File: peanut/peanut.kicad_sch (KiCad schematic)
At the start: 35 parts, among them J1 USB-C, Q1 NMOS, U2 MS5611-01BA, U3 ESP32-C3FH4, Y2 40MHz

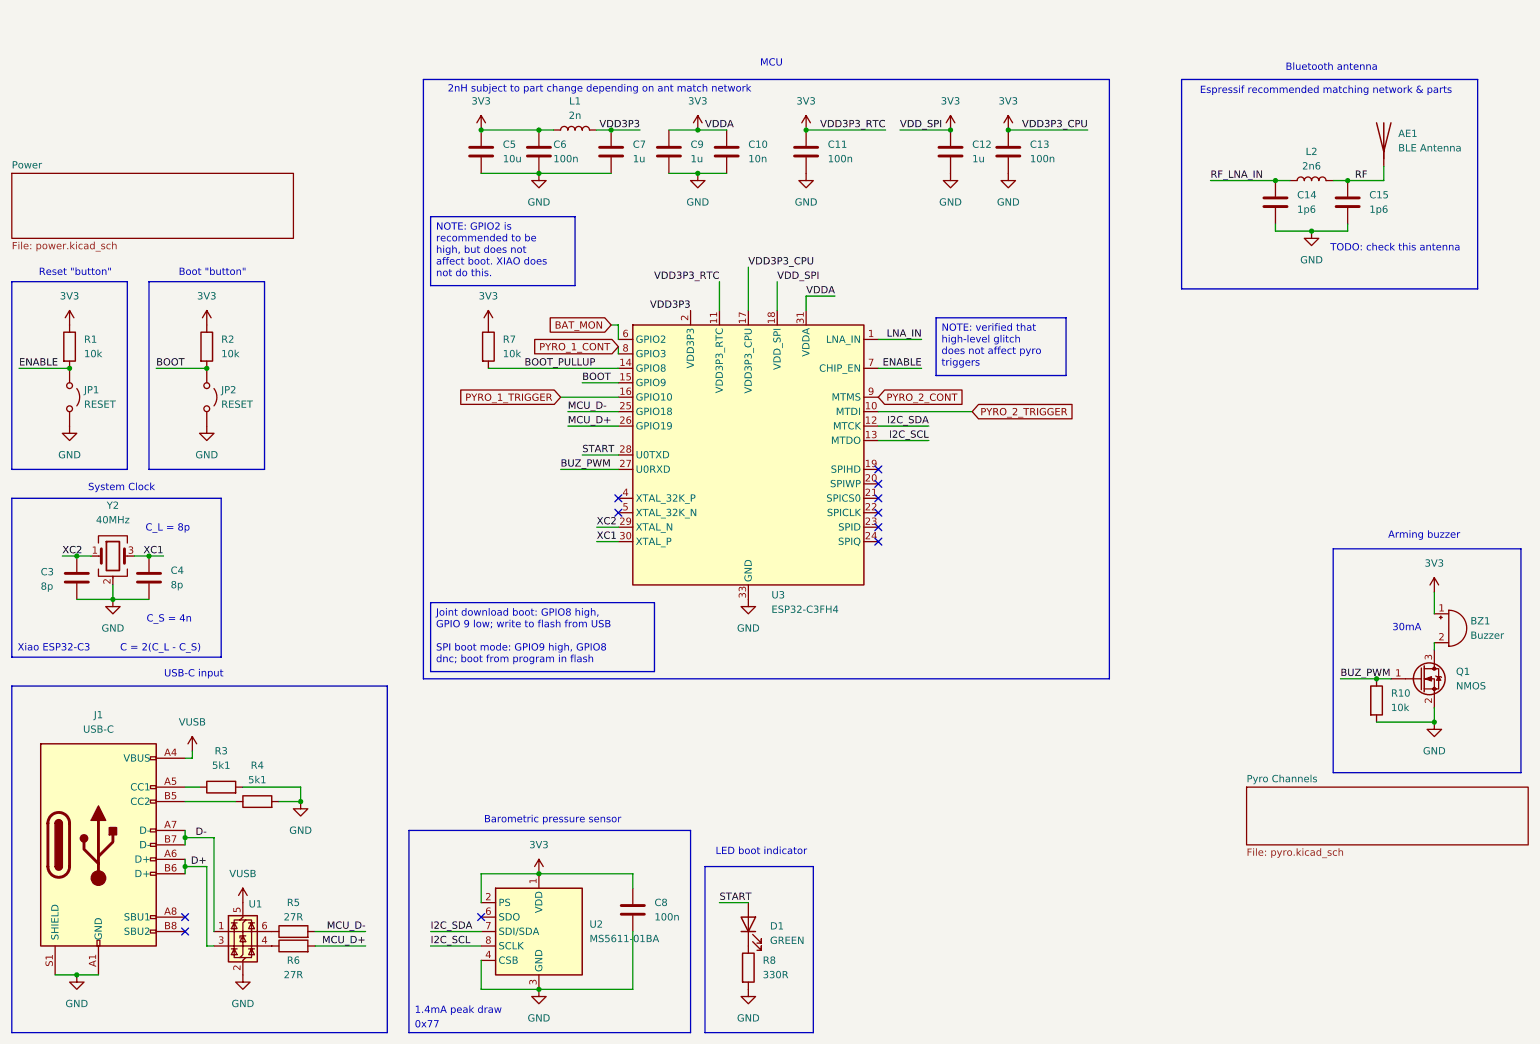
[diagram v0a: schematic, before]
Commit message: feat: Mounting holes
Added M3 mounting holes.
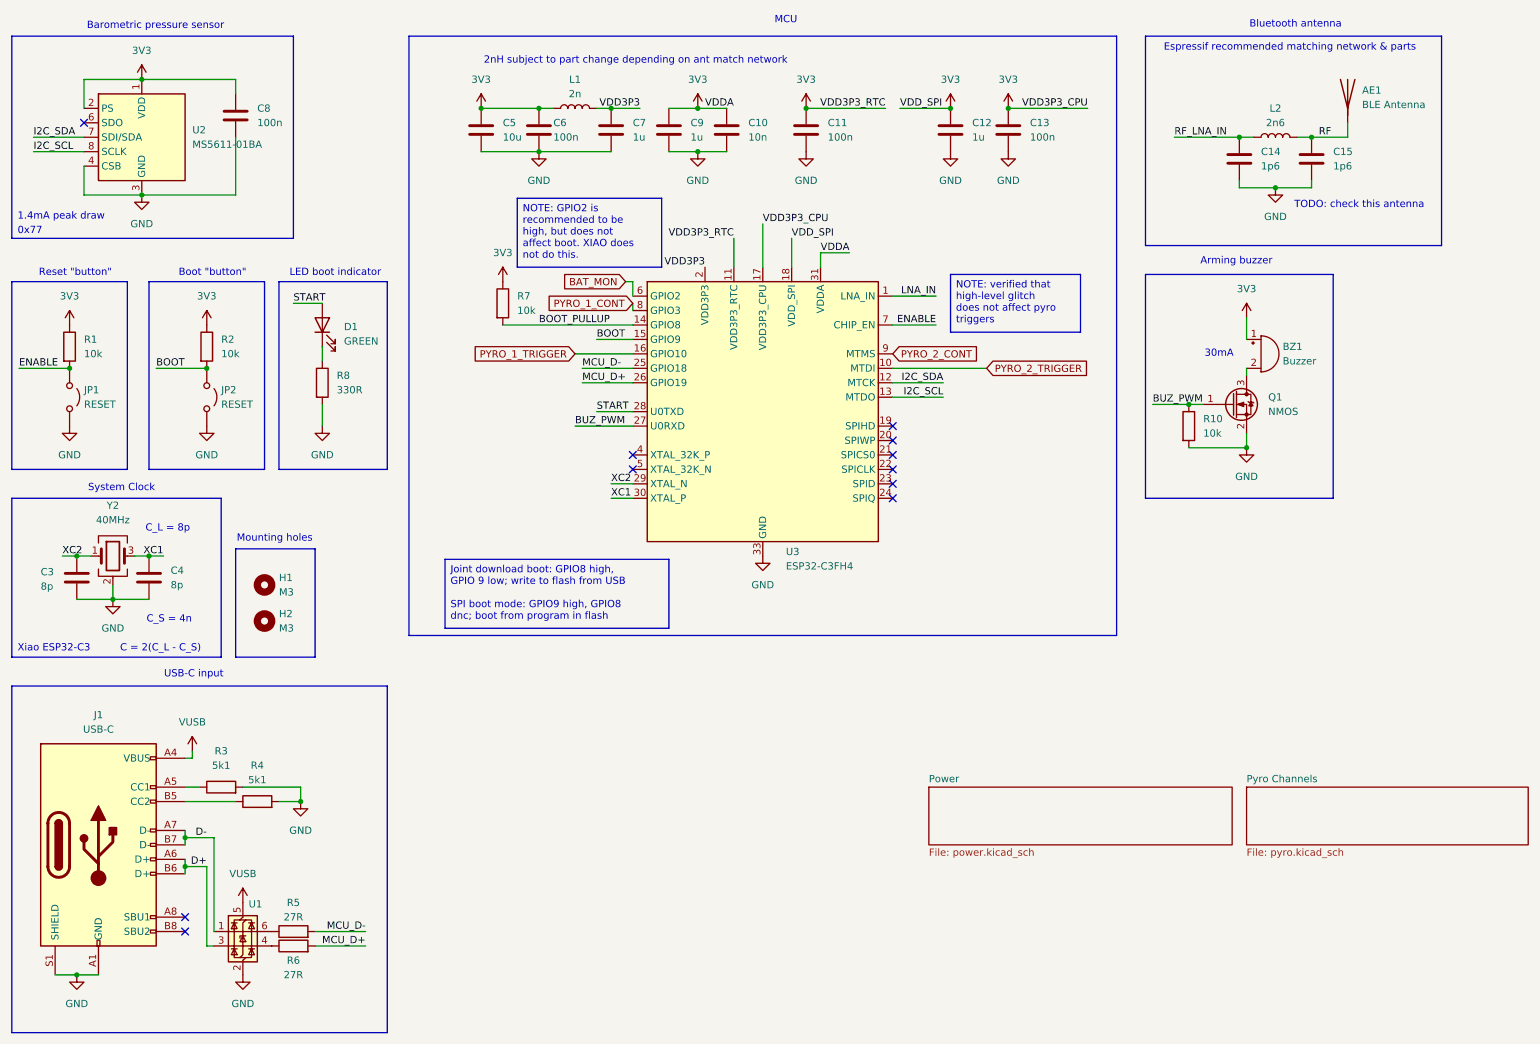
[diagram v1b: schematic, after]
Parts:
- added H1, H2: M3, MountingHole:MountingHole_3.2mm_M3_DIN965_Pad_TopOnly, symbol Mechanical:MountingHole
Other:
- note added: "Mounting holes"
- moved on the sheet: AE1, BZ1, C10, C11, C12, C13, C14, C15, C5, C6, C7, C8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

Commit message: feat: Better layout
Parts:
- renumbered C3 to C1, C12 to C10, C13 to C11, C14 to C12, C15 to C13, C4 to C2, C8 to C3, C5 to C4, C6 to C5, C7 to C6, C9 to C7, C10 to C8, C11 to C9, R8 to R7, R7 to R8, R10 to R9, U2 to U1, U1 to U2, Y2 to Y1
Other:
- note added: "M3 mounting"
- note removed: "Mounting holes"
- moved on the sheet: H1, H2

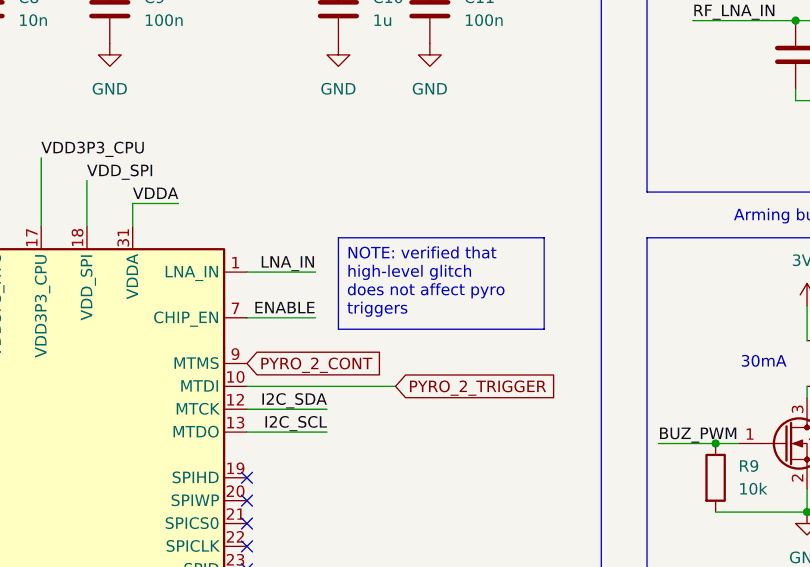
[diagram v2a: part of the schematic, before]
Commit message: feat: Added necessary silkscreen information
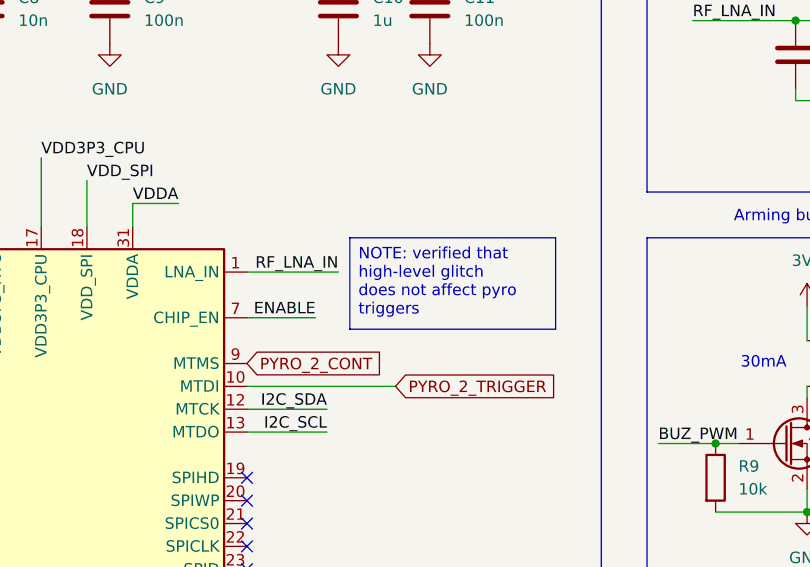
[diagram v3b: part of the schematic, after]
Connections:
- net LNA_IN is gone; now on net RF_LNA_IN: U3.1 (LNA_IN)
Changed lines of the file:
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@@
 	(text_box "NOTE: verified that high-level glitch does not affect pyro triggers"
 		(exclude_from_sim no)
-		(at 180.34 62.23 0)
+		(at 181.61 62.23 0)
 		(size 22.86 10.16)
 		(margins 0.9525 0.9525 0.9525 0.9525)
@@
 	(wire
 		(pts
-			(xy 177.8 66.04) (xy 170.18 66.04)
+			(xy 180.34 66.04) (xy 170.18 66.04)
 		)
 		(stroke
@@
 		)
 	)
-	(label "LNA_IN"
-		(at 177.8 66.04 180)
-		(effects
-			(font
+	(label "RF_LNA_IN"
+		(at 180.34 66.04 180)
+		(effects
+			(font

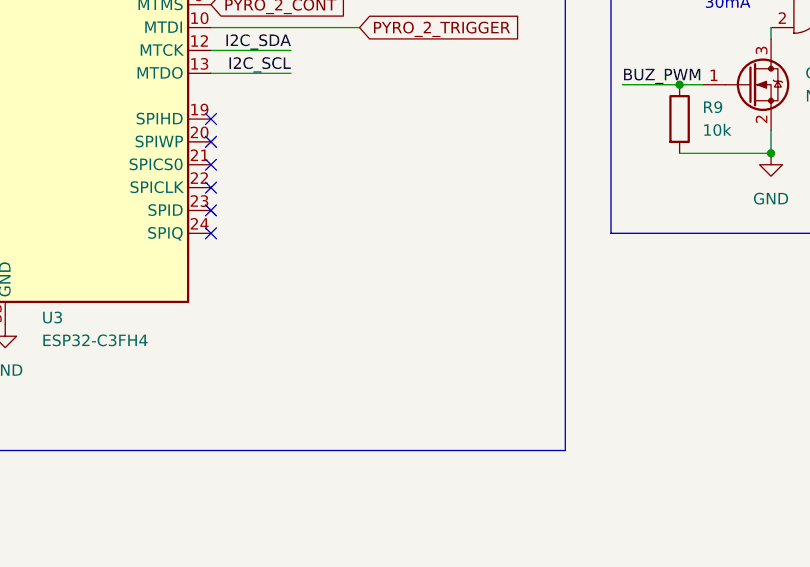
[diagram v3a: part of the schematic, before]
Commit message: feat: Added inner layer pours
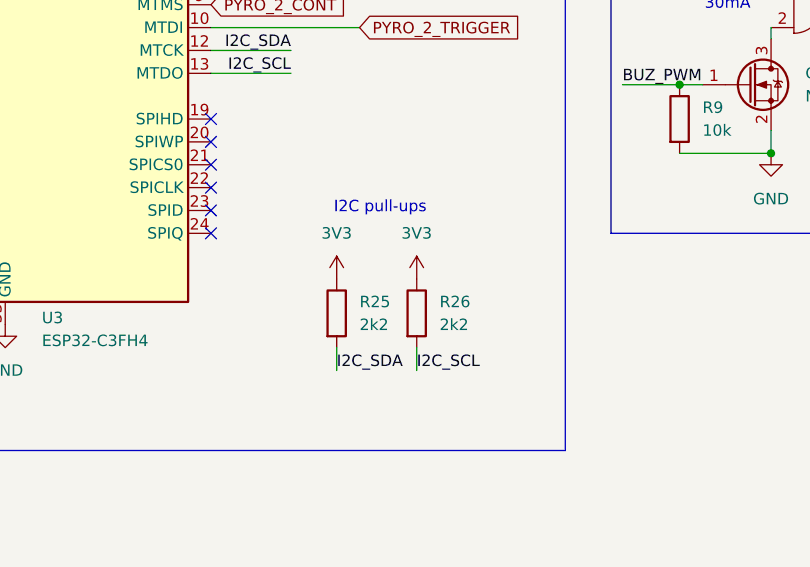
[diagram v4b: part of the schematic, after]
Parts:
- added R25, R26: 2k2, Resistor_SMD:R_0402_1005Metric, symbol Device:R
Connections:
- net 3V3: now also R25.1, R26.1
- net I2C_SCL: now also R26.2
- net I2C_SDA: now also R25.2
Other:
- note added: "I2C pull-ups"

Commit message: feat: 100n capacitors to 0603
Since there is sufficient space, the 100n capacitors have been increased
to 0603 size and all placed on the back of the board. This allows the
board to be squished in further slightly.
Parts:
- C11, C3, C5, C9: footprint Capacitor_SMD:C_0402_1005Metric -> Capacitor_SMD:C_0603_1608Metric; MPN GRM155R61A104KA01J -> KGM15AR70J104KT
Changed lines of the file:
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@@
 			)
 		)
-		(property "Footprint" "Capacitor_SMD:C_0402_1005Metric"
+		(property "Footprint" "Capacitor_SMD:C_0603_1608Metric"
 			(at 191.4652 40.64 0)
 			(hide yes)
@@
 			)
 		)
-		(property "Datasheet" ""
+		(property "Datasheet" "https://ele.kyocera.com/assets/products/capacitor/KGM_Series_e.pdf"
 			(at 190.5 36.83 0)
 			(hide yes)
@@
 			)
 		)
-		(property "MPN" "GRM155R61A104KA01J"
+		(property "MPN" "KGM15AR70J104KT"
 			(at 190.5 36.83 0)
 			(hide yes)
@@
 			)
 		)
-		(property "Footprint" "Capacitor_SMD:C_0402_1005Metric"
+		(property "Footprint" "Capacitor_SMD:C_0603_1608Metric"
 			(at 155.9052 40.64 0)
 			(hide yes)
@@
 			)
 		)
-		(property "Datasheet" ""
+		(property "Datasheet" "https://ele.kyocera.com/assets/products/capacitor/KGM_Series_e.pdf"
 			(at 154.94 36.83 0)
 			(hide yes)
@@
 			)
 		)
-		(property "MPN" "GRM155R61A104KA01J"
+		(property "MPN" "KGM15AR70J104KT"
 			(at 154.94 36.83 0)
 			(hide yes)
@@
 			)
 		)
-		(property "Footprint" "Capacitor_SMD:C_0402_1005Metric"
+		(property "Footprint" "Capacitor_SMD:C_0603_1608Metric"
 			(at 55.5752 38.1 0)
 			(hide yes)
@@
 			)
 		)
-		(property "Datasheet" ""
+		(property "Datasheet" "https://ele.kyocera.com/assets/products/capacitor/KGM_Series_e.pdf"
 			(at 54.61 34.29 0)
 			(hide yes)
@@
 			)
 		)
-		(property "MPN" "GRM155R61A104KA01J"
+		(property "MPN" "KGM15AR70J104KT"
 			(at 54.61 34.29 0)
 			(hide yes)
@@
 			)
 		)
-		(property "Footprint" "Capacitor_SMD:C_0402_1005Metric"
+		(property "Footprint" "Capacitor_SMD:C_0603_1608Metric"
 			(at 108.9152 40.64 0)
 			(hide yes)
@@
 			)
 		)
-		(property "Datasheet" ""
+		(property "Datasheet" "https://ele.kyocera.com/assets/products/capacitor/KGM_Series_e.pdf"
 			(at 107.95 36.83 0)
 			(hide yes)
@@
 			)
 		)
-		(property "MPN" "GRM155R61A104KA01J"
+		(property "MPN" "KGM15AR70J104KT"
 			(at 107.95 36.83 0)
 			(hide yes)
